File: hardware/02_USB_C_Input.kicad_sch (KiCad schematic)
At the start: 12 parts, among them J1 USB_C_Receptacle_USB2.0_16P, U1 USBLC6-2SC6

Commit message: Pre-layout finalization and second design review pass (Rev A)
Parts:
- C1, C3, C4: footprint (none) -> Capacitor_SMD:C_0603_1608Metric; LCSC Part (none) -> C14663
- C2: footprint (none) -> Capacitor_SMD:C_0805_2012Metric; LCSC Part (none) -> C15850
- D1: value D_Zener -> SMF5.0A; footprint (none) -> Diode_SMD:D_SOD-123F; LCSC Part (none) -> C2980403
- F1: value Fuse -> 1206L075/16WR; footprint (none) -> Fuse:Fuse_1206_3216Metric; LCSC Part (none) -> C371166
- J1: footprint (none) -> Connector_USB:USB_C_Receptacle_HRO_TYPE-C-31-M-12; LCSC Part (none) -> C165948
- R1, R2: footprint (none) -> Resistor_SMD:R_0603_1608Metric; LCSC Part (none) -> C23345
- R3, R4: footprint (none) -> Resistor_SMD:R_0603_1608Metric; LCSC Part (none) -> C23186
- U1: LCSC Part (none) -> C7519
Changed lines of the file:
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@@
 			)
 		)
-		(property "Value" "Fuse"
+		(property "Value" "1206L075/16WR"
 			(at 123.19 39.37 90)
 			(show_name no)
@@
 			)
 		)
-		(property "Footprint" ""
+		(property "Footprint" "Fuse:Fuse_1206_3216Metric"
 			(at 123.19 44.958 90)
 			(hide yes)
@@
 		(property "Description" "Fuse"
 			(at 123.19 43.18 0)
+			(hide yes)
+			(show_name no)
+			(do_not_autoplace no)
+			(effects
+				(font
+					(size 1.27 1.27)
+				)
+			)
+		)
+		(property "LCSC Part" "C371166"
+			(at 123.19 43.18 90)
 			(hide yes)
 			(show_name no)
@@
 			)
 		)
-		(property "Footprint" ""
+		(property "Footprint" "Capacitor_SMD:C_0603_1608Metric"
 			(at 145.0848 74.93 0)
 			(hide yes)
@@
 		(property "Purpose" ""
 			(at 146.05 78.74 0)
+			(show_name no)
+			(do_not_autoplace no)
+			(effects
+				(font
+					(size 1.27 1.27)
+				)
+			)
+		)
+		(property "LCSC Part" "C14663"
+			(at 146.05 78.74 0)
+			(hide yes)
 			(show_name no)
 			(do_not_autoplace no)
@@
 			)
 		)
-		(property "Footprint" ""
+		(property "Footprint" "Resistor_SMD:R_0603_1608Metric"
 			(at 129.54 86.868 90)
 			(hide yes)
@@
 		(property "Description" "Resistor"
 			(at 129.54 85.09 0)
+			(hide yes)
+			(show_name no)
+			(do_not_autoplace no)
+			(effects
+				(font
+					(size 1.27 1.27)
+				)
+			)
+		)
+		(property "LCSC Part" "C23345"
+			(at 129.54 85.09 90)
 			(hide yes)
 			(show_name no)
@@
 			)
 		)
-		(property "Footprint" ""
+		(property "Footprint" "Capacitor_SMD:C_0603_1608Metric"
 			(at 123.19 58.7248 0)
 			(hide yes)
@@
 		(property "Description" "Unpolarized capacitor"
 			(at 119.38 59.69 0)
+			(hide yes)
+			(show_name no)
+			(do_not_autoplace no)
+			(effects
+				(font
+					(size 1.27 1.27)
+				)
+			)
+		)
+		(property "LCSC Part" "C14663"
+			(at 119.38 59.69 90)
 			(hide yes)
 			(show_name no)
@@
 			)
 		)
-		(property "Footprint" ""
+		(property "Footprint" "Resistor_SMD:R_0603_1608Metric"
 			(at 129.54 84.328 90)
 			(hide yes)
@@
 		(property "Description" "Resistor"
 			(at 129.54 82.55 0)
+			(hide yes)
+			(show_name no)
+			(do_not_autoplace no)
+			(effects
+				(font
+					(size 1.27 1.27)
+				)
+			)
+		)
+		(property "LCSC Part" "C23345"
+			(at 129.54 82.55 90)
 			(hide yes)
 			(show_name no)
@@
 		)
 		(property "Description" "Very low capacitance ESD protection diode, 2 data-line, SOT-23-6"
+			(at 115.57 82.55 0)
+			(hide yes)
+			(show_name no)
+			(do_not_autoplace no)
+			(effects
+				(font
+					(size 1.27 1.27)
+				)
+			)
+		)
+		(property "LCSC Part" "C7519"
 			(at 115.57 82.55 0)
 			(hide yes)
@@
 			)
 		)
-		(property "Footprint" ""
+		(property "Footprint" "Resistor_SMD:R_0603_1608Metric"
 			(at 145.542 52.07 90)
 			(hide yes)
@@
 		(property "Purpose" ""
 			(at 147.32 52.07 0)
+			(show_name no)
+			(do_not_autoplace no)
+			(effects
+				(font
+					(size 1.27 1.27)
+				)
+			)
+		)
+		(property "LCSC Part" "C23186"
+			(at 147.32 52.07 0)
+			(hide yes)
 			(show_name no)
 			(do_not_autoplace no)
@@
 			)
 		)
-		(property "Value" "D_Zener"
+		(property "Value" "SMF5.0A"
 			(at 97.79 101.5999 90)
 			(show_name no)
@@
 			)
 		)
-		(property "Footprint" ""
+		(property "Footprint" "Diode_SMD:D_SOD-123F"
 			(at 95.25 100.33 0)
 			(hide yes)
@@
 		(property "Description" "Zener diode"
 			(at 95.25 100.33 0)
+			(hide yes)
+			(show_name no)
+			(do_not_autoplace no)
+			(effects
+				(font
+					(size 1.27 1.27)
+				)
+			)
+		)
+		(property "LCSC Part" "C2980403"
+			(at 95.25 100.33 90)
 			(hide yes)
 			(show_name no)
@@
 			)
 		)
-		(property "Footprint" ""
+		(property "Footprint" "Resistor_SMD:R_0603_1608Metric"
 			(at 134.112 54.61 90)
 			(hide yes)
@@
 		)
 		(property "Description" "Resistor"
+			(at 135.89 54.61 0)
+			(hide yes)
+			(show_name no)
+			(do_not_autoplace no)
+			(effects
+				(font
+					(size 1.27 1.27)
+				)
+			)
+		)
+		(property "LCSC Part" "C23186"
 			(at 135.89 54.61 0)
 			(hide yes)
@@
 			)
 		)
-		(property "Footprint" ""
+		(property "Footprint" "Capacitor_SMD:C_0805_2012Metric"
 			(at 141.2748 33.02 0)
 			(hide yes)
@@
 		)
 		(property "Description" "Unpolarized capacitor"
+			(at 142.24 36.83 0)
+			(hide yes)
+			(show_name no)
+			(do_not_autoplace no)
+			(effects
+				(font
+					(size 1.27 1.27)
+				)
+			)
+		)
+		(property "LCSC Part" "C15850"
 			(at 142.24 36.83 0)
 			(hide yes)
@@
 			)
 		)
-		(property "Footprint" ""
+		(property "Footprint" "Connector_USB:USB_C_Receptacle_HRO_TYPE-C-31-M-12"
 			(at 76.2 58.42 0)
 			(hide yes)
@@
 		)
 		(property "Description" "USB 2.0-only 16P Type-C Receptacle connector"
+			(at 72.39 58.42 0)
+			(hide yes)
+			(show_name no)
+			(do_not_autoplace no)
+			(effects
+				(font
+					(size 1.27 1.27)
+				)
+			)
+		)
+		(property "LCSC Part" "C165948"
 			(at 72.39 58.42 0)
 			(hide yes)
@@
 			)
 		)
-		(property "Footprint" ""
+		(property "Footprint" "Capacitor_SMD:C_0603_1608Metric"
 			(at 145.0848 85.09 0)
 			(hide yes)
@@
 			(show_name no)
 			(do_not_autoplace no)
+			(effects
+				(font
+					(size 1.27 1.27)
+				)
+			)
+		)
+		(property "LCSC Part" "C14663"
+			(at 146.05 88.9 0)
+			(hide yes)
+			(show_name no)
+			(do_not_autoplace no)

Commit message: J1: project-local USB-C footprint, lower shield-leg drill 1.2->1.4 per HRO drawing
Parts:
- J1: footprint Connector_USB:USB_C_Receptacle_HRO_TYPE-C-31-M-12 -> PlantMonitor_JLC:USB_C_Receptacle_HRO_TYPE-C-31-M-12
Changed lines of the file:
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@@
 			)
 		)
-		(property "Footprint" "Connector_USB:USB_C_Receptacle_HRO_TYPE-C-31-M-12"
+		(property "Footprint" "PlantMonitor_JLC:USB_C_Receptacle_HRO_TYPE-C-31-M-12"
 			(at 76.2 58.42 0)
 			(hide yes)
@@
 			(show_name no)
 			(do_not_autoplace no)
+			(effects
+				(font
+					(size 1.27 1.27)
+				)
+			)
+		)
+		(property "Purpose" ""
+			(at 72.39 58.42 0)
+			(show_name no)
+			(do_not_autoplace no)

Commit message: Snapshot before 3D model path rework
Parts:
- D1: footprint Diode_SMD:D_SOD-123F -> PlantMonitor_JLC:D_SOD-123F
- F1: footprint Fuse:Fuse_1206_3216Metric -> PlantMonitor_JLC:Fuse_1206_3216Metric
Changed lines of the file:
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@@
 			)
 		)
-		(property "Footprint" "Fuse:Fuse_1206_3216Metric"
+		(property "Footprint" "PlantMonitor_JLC:Fuse_1206_3216Metric"
 			(at 123.19 44.958 90)
 			(hide yes)
@@
 			)
 		)
-		(property "Footprint" "Diode_SMD:D_SOD-123F"
+		(property "Footprint" "PlantMonitor_JLC:D_SOD-123F"
 			(at 95.25 100.33 0)
 			(hide yes)

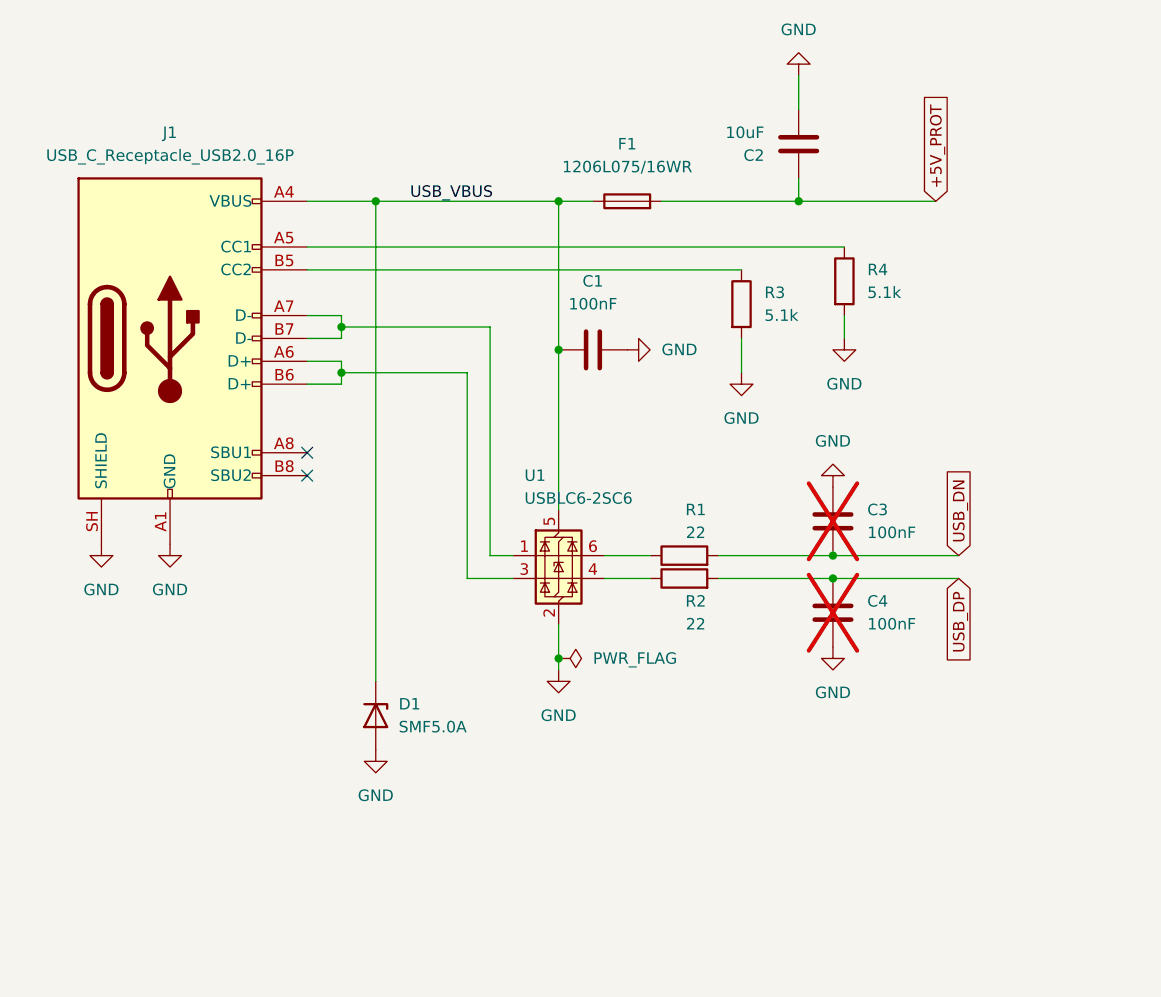
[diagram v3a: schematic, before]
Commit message: Placement fixes; rounded board corners (R4.25)
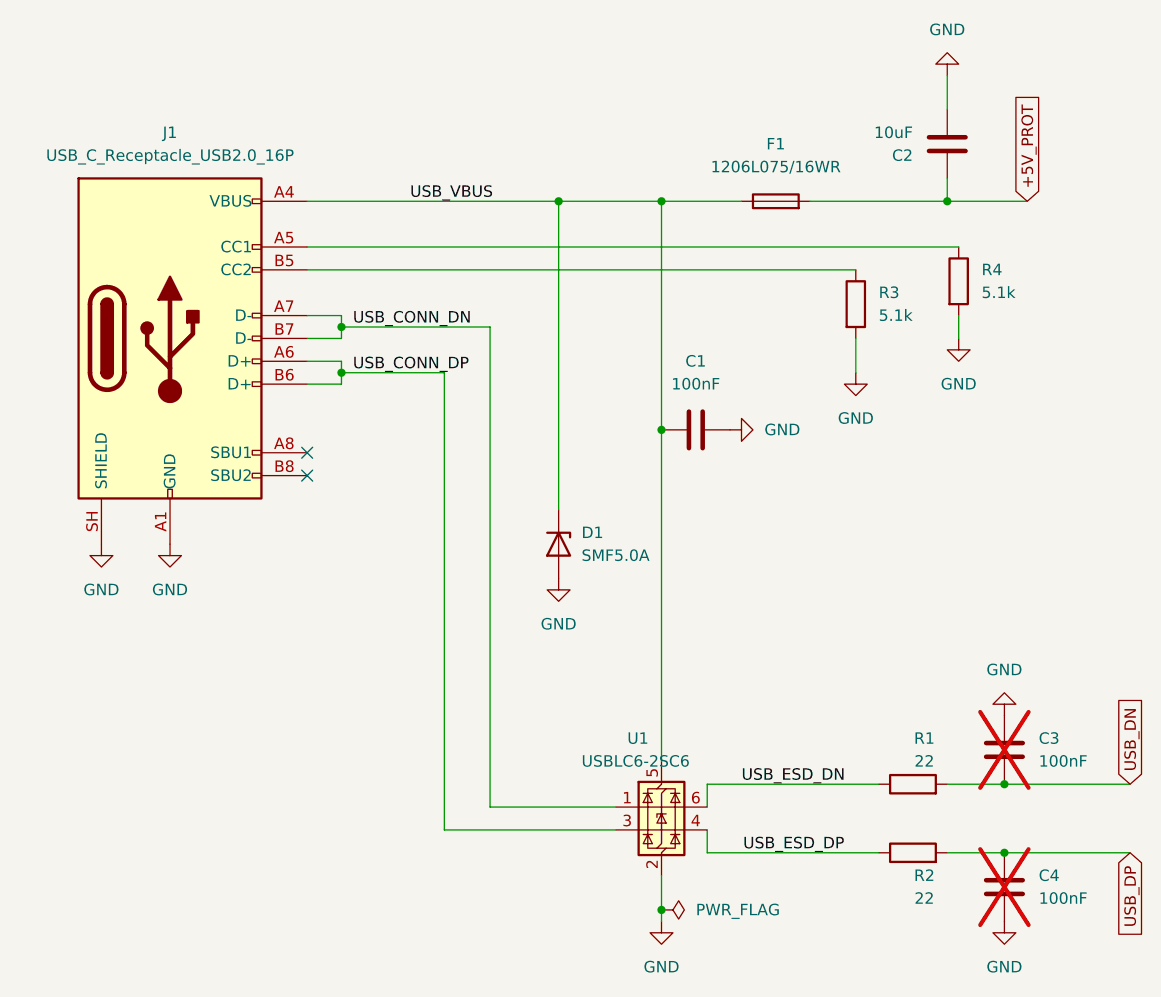
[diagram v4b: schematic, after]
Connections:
- net USB_ESD_DP: now reaches R2.1, U1.4 (I/O2)
- net USB_ESD_DN: now reaches R1.1, U1.6 (I/O1)
- net USB_CONN_DN: now reaches J1.A7 (D-), J1.B7 (D-), U1.1 (I/O1)
- net USB_CONN_DP: now reaches J1.A6 (D+), J1.B6 (D+), U1.3 (I/O2)
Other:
- moved on the sheet: C1, C2, C3, C4, D1, F1, R1, R2, R3, R4, U1

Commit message: DRC and ERC cleanup
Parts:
- C3, C4: now left out of the parts list
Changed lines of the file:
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@@
 		(body_style 1)
 		(exclude_from_sim no)
-		(in_bom yes)
+		(in_bom no)
 		(on_board yes)
 		(in_pos_files yes)
@@
 		(body_style 1)
 		(exclude_from_sim no)
-		(in_bom yes)
-		(on_board yes)
-		(in_pos_files yes)
+		(in_bom no)
+		(on_board yes)
+		(in_pos_files yes)

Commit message: pre-order baseline
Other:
- company: (none) -> MuffinByteLabs
- title: 02_USB_C_Input -> ESP32-S3 Plant Monitor
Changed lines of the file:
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@@
 	(paper "A4")
 	(title_block
-		(title "02_USB_C_Input")
-		(date "2026-07-03")
+		(title "ESP32-S3 Plant Monitor")
+		(date "2026-08-21")
 		(rev "A")
+		(company "MuffinByteLabs")
+		(comment 1 "Designed by Ray Malik")
+		(comment 2 "4-layer JLC04161H-7628, 1.6 mm, HASL lead-free, green mask")
+		(comment 3 "Fabrication and assembly: JLCPCB")
 	)
 	(junction
